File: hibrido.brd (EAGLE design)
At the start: 84 x 62 mm, 14 parts

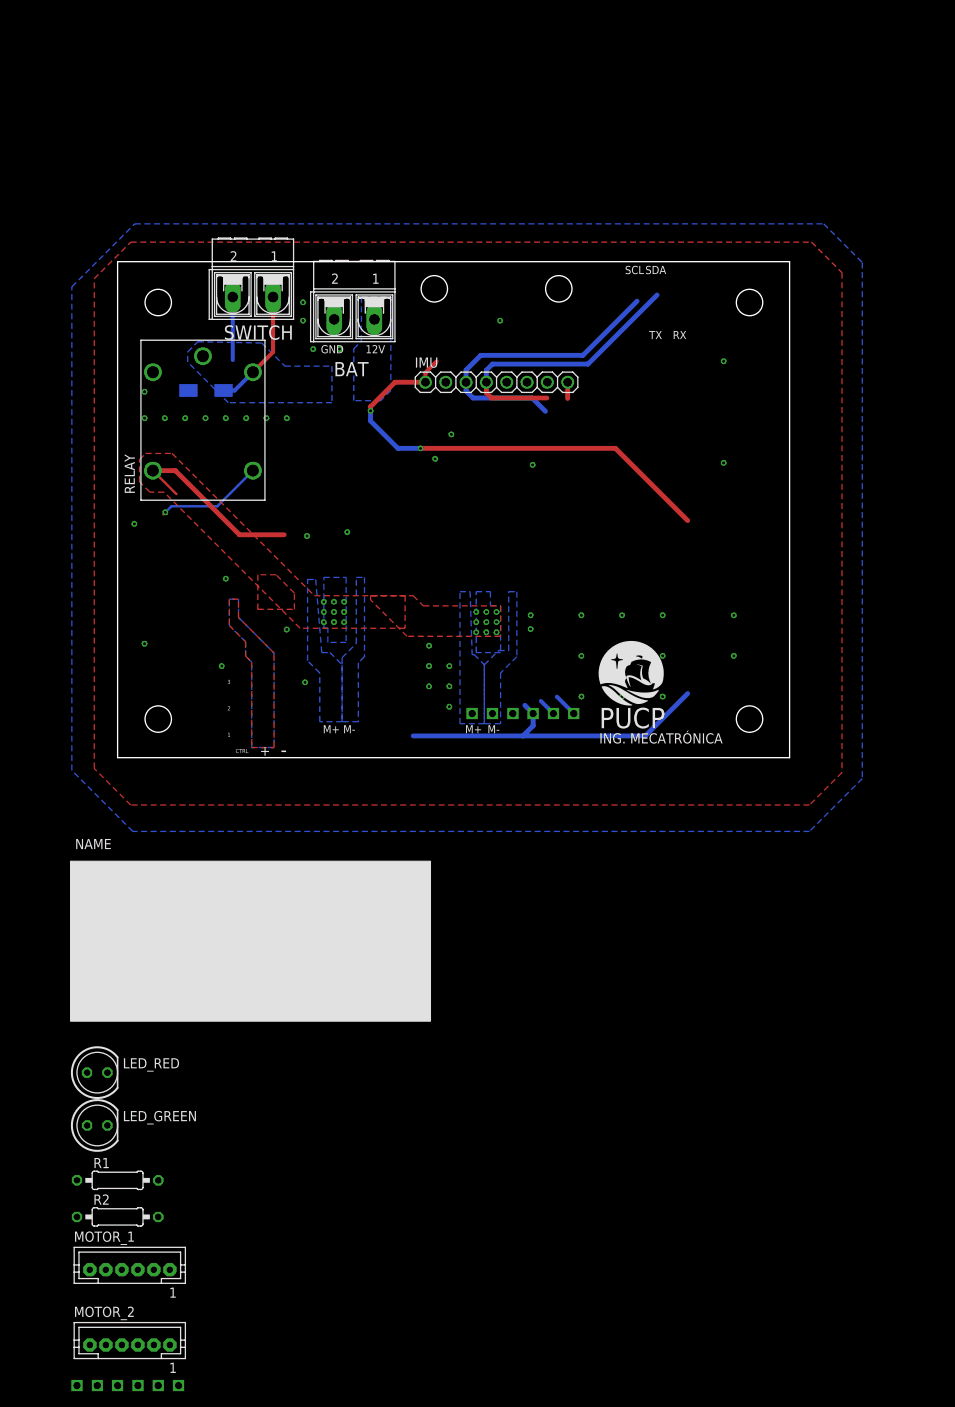
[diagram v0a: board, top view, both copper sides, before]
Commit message: Hibrido casi terminado, sin considerar comunicación entre ESPs
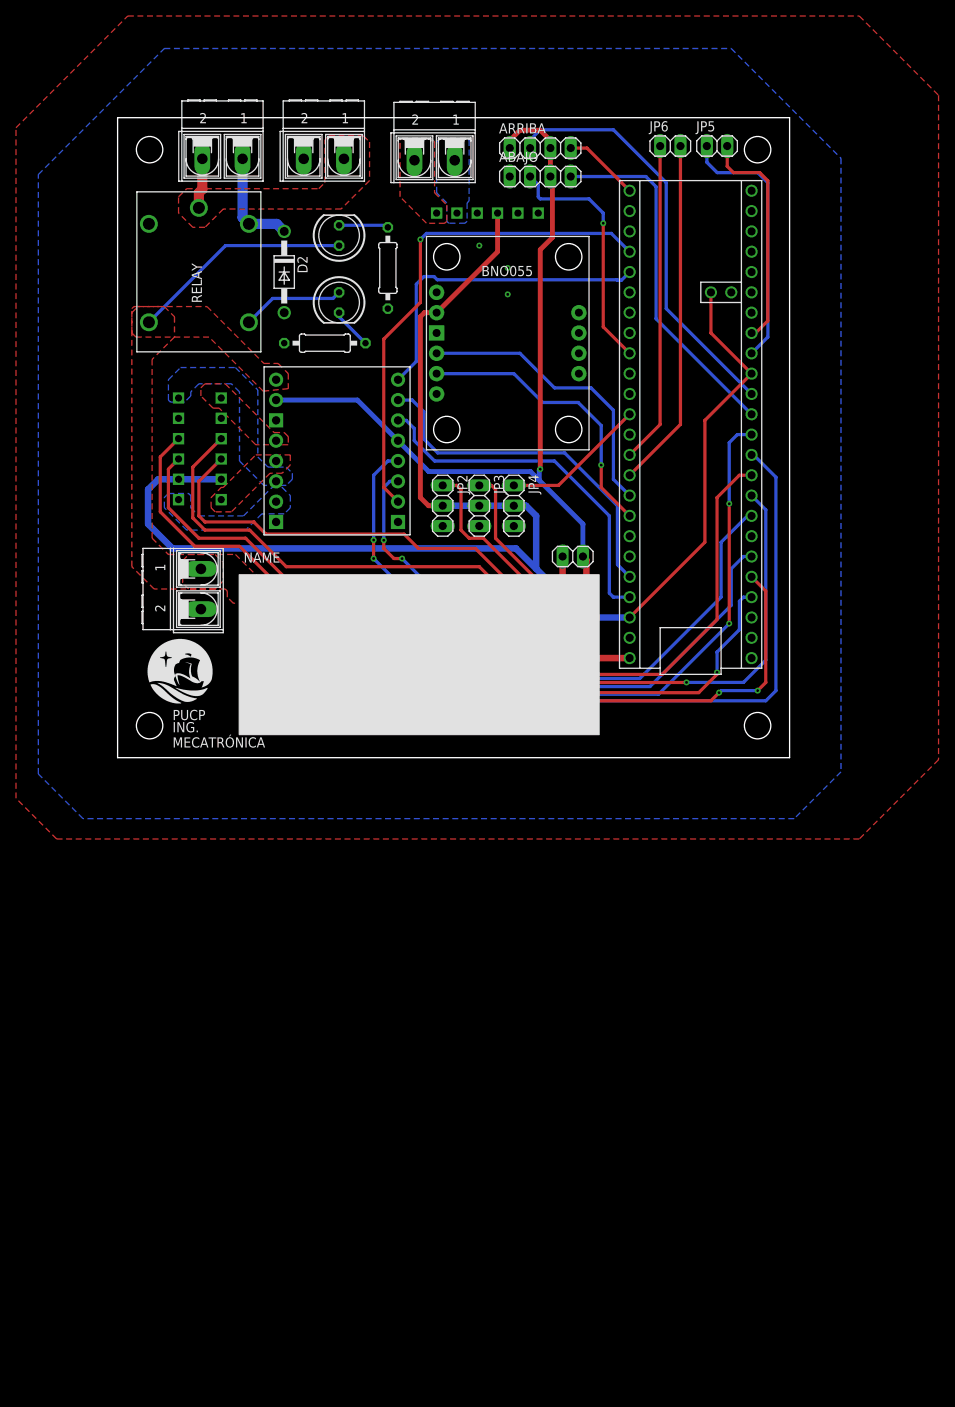
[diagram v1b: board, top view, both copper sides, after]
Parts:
- removed D1: M2, SamacSys_Parts:DIOM5327X250N
- removed IMU: (no value), MPU6050:MPU6050
- removed MOTOR2: MOTOR_JGB370, MOTOR_JGB370:MOTOR_JGB370
- removed MOTOR_1, MOTOR_2: (no value), jst-ph:JST-PH6
- added A1: TEENSY_4.1, TEENSY_4.1:TEENSY_LONG_EXT
- added ABAJO, ARRIBA: (no value), pinhead:1X04
- added ALIMENTACION_DRIVER, DRIVER_HIBRIDACION: (no value), con-ptr500:AK500/2-H
- added BNO055: BNO055, BNO055:BNO055
- added D2: 1N4004, diode:DO41-10
- added JP1, JP5, JP6: (no value), pinhead:1X02
- added JP2, JP3, JP4: (no value), pinhead:1X03
- added MOTOR3, MOTOR5: MOTOR_JGB370, MOTOR_JGB370:MOTOR_JGB370
- added U$3: TB6612FNG, TB6612FNG:TB6612FNG
- moved MOTOR1 152.6 mm to (45.0, 68.1), turned to 180 degrees
- moved R2 123.3 mm to (33.8, 61.2), turned to 90 degrees
- moved LED_GREEN 115.3 mm to (27.7, 65.3), turned to 90 degrees
- moved R1 107.8 mm to (25.9, 51.8)
- moved LED_RED 100.9 mm to (27.7, 56.9), turned to 270 degrees
- moved U$2 41.6 mm to (38.6, 14.2)
- moved BAT 20.4 mm to (25.8, 74.9)
- moved RELAY 18.5 mm to (2.41, 50.7)
- moved SWITCH 17.7 mm to (13.1, 74.9)
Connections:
- net ENAM1 renamed C1_H
- net ENBM1 renamed C2_H
- removed net +3V3: IMU.1, MOTOR1.+5V, MOTOR2.+5V, MOTOR_1.5, MOTOR_2.5
- removed net 16.8V: LED_GREEN.A, RELAY.NO, U$2.IN+
- removed net ENAM2: MOTOR2.ENCB
- removed net ENBM2: MOTOR2.ENCA
- removed net INT_MPU: IMU.8
- removed net MA_1: MOTOR1.MOTOR-
- removed net MA_2: MOTOR2.MOTOR-
- removed net MB_1: MOTOR1.MOTOR+
- removed net MB_2: MOTOR2.MOTOR+
- new net 12V: ALIMENTACION_DRIVER.1, LED_GREEN.A, RELAY.NO, U$2.IN+, U$3.1
- new net 14: A1.D14, JP4.1
- new net 16: A1.D16, JP6.1
- new net 17: A1.D17, JP6.2
- new net 24: A1.D24, JP5.1
- new net 25: A1.D25, JP5.2
- new net 3V3: A1.3V3, A1.3V3@2, A1.3V3@3, BNO055.2, JP2.2, JP3.2, JP4.2, MOTOR1.+5V, MOTOR3.ENCA, MOTOR5.ENCA
- new net 5V: ABAJO.3, ARRIBA.1, ARRIBA.3, JP1.2, U$2.OUT+, U$3.12, U$3.2
- new net 7: A1.D7, JP2.1
- new net 8: A1.D8, JP3.1
- new net AI1: A1.D23, U$3.11
- new net AI2: A1.D22, U$3.10
- new net BI1: A1.D9, U$3.13
- new net BI2: A1.D10, U$3.14
- new net LPWM: A1.D11, ABAJO.4
- new net L_IS: A1.D41, ABAJO.2
- new net N$1: LED_RED.K, R1.2
- new net N$10: A1.D28
- new net N$11: A1.D13
- new net N$19: A1.D5
- new net N$2: A1.D34
- new net N$24: A1.D21
- new net N$25: A1.D20
- new net N$3: A1.D35
- new net N$30: A1.D15
- new net N$33: A1.D40
- new net N$34: A1.D39
- new net N$35: A1.D38
- new net N$38: A1.D26
- new net N$39: A1.D27
- new net N$4: LED_GREEN.K, R2.2
- new net N$6: A1.D32
- new net N$7: A1.D31
- new net N$8: A1.D30
- new net N$9: A1.D29
- new net OUTA: DRIVER_HIBRIDACION.2, MOTOR1.MOTOR+
- new net OUTB: DRIVER_HIBRIDACION.1, MOTOR1.MOTOR-
- new net PWMA: A1.D37, U$3.9
- new net PWMB: A1.D36, U$3.15
- new net RPWM: A1.D33, ARRIBA.4
- new net R_IS: A1.D12, ARRIBA.2
- new net VBAT: A1.VBAT
- new net VIN_TEENSY: A1.VIN, JP1.1
- net A01: now also MOTOR3.MOTOR+, U$3.4; no longer MOTOR_1.1
- net A02: now also MOTOR3.ENCB, U$3.5; no longer MOTOR_1.6
- net B01: now also MOTOR5.ENCB, U$3.7; no longer MOTOR_2.6
- net B02: now also MOTOR5.MOTOR+, U$3.6; no longer MOTOR_2.1
- net C1_L: now also A1.D6, MOTOR5.GND; no longer MOTOR_2.3
- net C1_R: now also A1.D3, MOTOR3.GND; no longer MOTOR_1.3
- net C2_L: now also A1.D4, MOTOR5.+5V; no longer MOTOR_2.4
- net C2_R: now also A1.D2, MOTOR3.+5V; no longer MOTOR_1.4
- net GND: now also A1.AGND/GND, A1.GND, A1.GND@2, ABAJO.1, ALIMENTACION_DRIVER.2, BNO055.3, D2.A, JP2.3, JP3.3, JP4.3, MOTOR3.MOTOR-, MOTOR5.MOTOR-, U$2.OUT-, U$3.16, U$3.3, U$3.8; no longer D1.2, IMU.2, MOTOR2.GND, MOTOR_1.2, MOTOR_2.2
- net SCL: now also A1.D19, BNO055.5; no longer IMU.3
- net SDA: now also A1.D18, BNO055.4; no longer IMU.4
- net VSWITCH: now also D2.C; no longer D1.1
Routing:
- net 3V3: track 0.00 -> 190.6 mm
- net C1_R: track 0.00 -> 115.0 mm, vias 0 -> 2
- net C1_L: track 0.00 -> 105.1 mm, vias 0 -> 1
- net 5V: track 0.00 -> 103.3 mm, vias 0 -> 1
- net BI1: track 0.00 -> 103.3 mm, vias 0 -> 2
- net C2_R: track 0.00 -> 102.5 mm, vias 0 -> 1
- net C2_L: track 0.00 -> 99.2 mm, vias 0 -> 1
- net +3V3: track 99.2 -> 0.00 mm, vias 2 -> 0
- net BI2: track 0.00 -> 89.9 mm, vias 0 -> 4
- net 7: track 0.00 -> 82.0 mm, vias 0 -> 1
- net 8: track 0.00 -> 71.5 mm
- net PWMB: track 0.00 -> 62.8 mm, vias 0 -> 1
- net R_IS: track 0.00 -> 52.1 mm
- net AI1: track 0.00 -> 44.7 mm
- net LPWM: track 0.00 -> 44.6 mm
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- added copper zone on layer 1, net 12V
- added copper zone on layer 1, net A01
- added copper zone on layer 1, net A02
- added copper zone on layer 16, net B01
- added copper zone on layer 16, net B02
- added copper zone on layer 1, net OUTA
- added copper zone on layer 16, net OUTB
- added copper zone on layer 1, net VIN
- removed copper zone on layer 1, net 16.8V
- removed copper zone on layer 16, net 16.8V
- removed copper zone on layer 1, net 6V
- removed copper zone on layer 16, net 6V
- removed copper zone on layer 16, net MA_1
- removed copper zone on layer 16, net MA_2
- removed copper zone on layer 16, net MB_1
- removed copper zone on layer 16, net MB_2
- removed copper zone on layer 16, net VIN
- removed copper zone on layer 16, net V_BAT
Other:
- board size 84 x 62 mm -> 84 x 80 mm
- board text removed: "+"
- board text removed: "-"
- board text removed: "1"
- board text removed: "12V"
- board text removed: "2"
- board text removed: "3"
- board text removed: "CTRL"
- board text removed: "DRIVER"
- board text removed: "GND"
- board text removed: "M+"
- board text removed: "M-"
- board text removed: "RX"
- board text removed: "SCL"
- board text removed: "SDA"
- board text removed: "TX"

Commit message: cambios casi finales
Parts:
- moved ALIMENTACION_DRIVER 0.76 mm to (10.4, 20.3)
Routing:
- net BI2: track 89.9 -> 90.8 mm
- net BI1: track 103.3 -> 104.1 mm
- net C1_L: track 105.1 -> 105.8 mm
- net C2_L: track 99.2 -> 99.8 mm

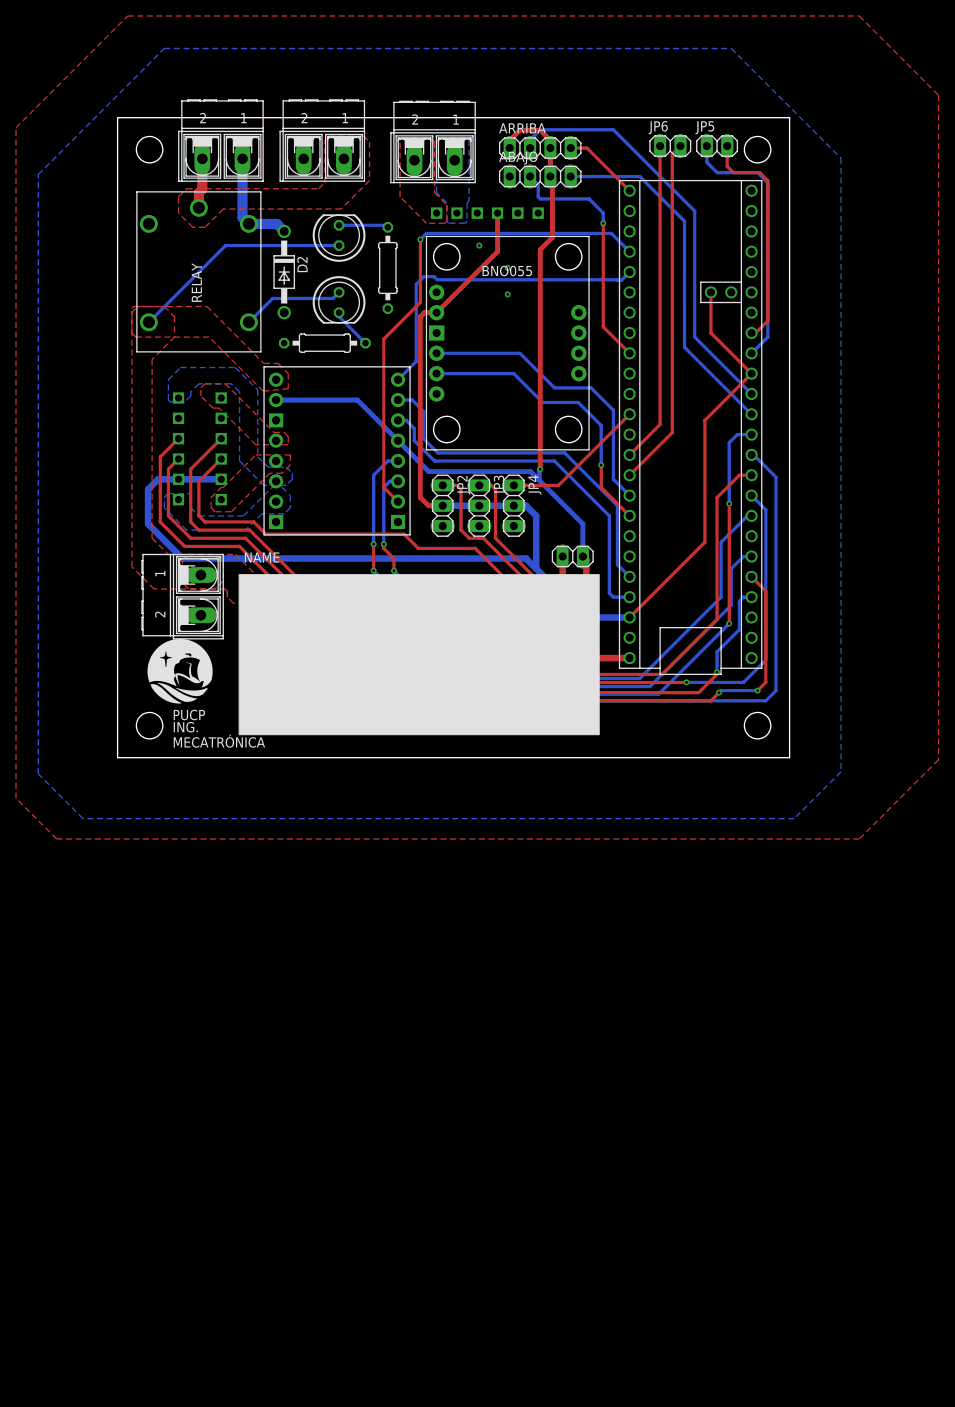
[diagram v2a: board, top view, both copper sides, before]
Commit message: PCB antes del cambio del drill vias
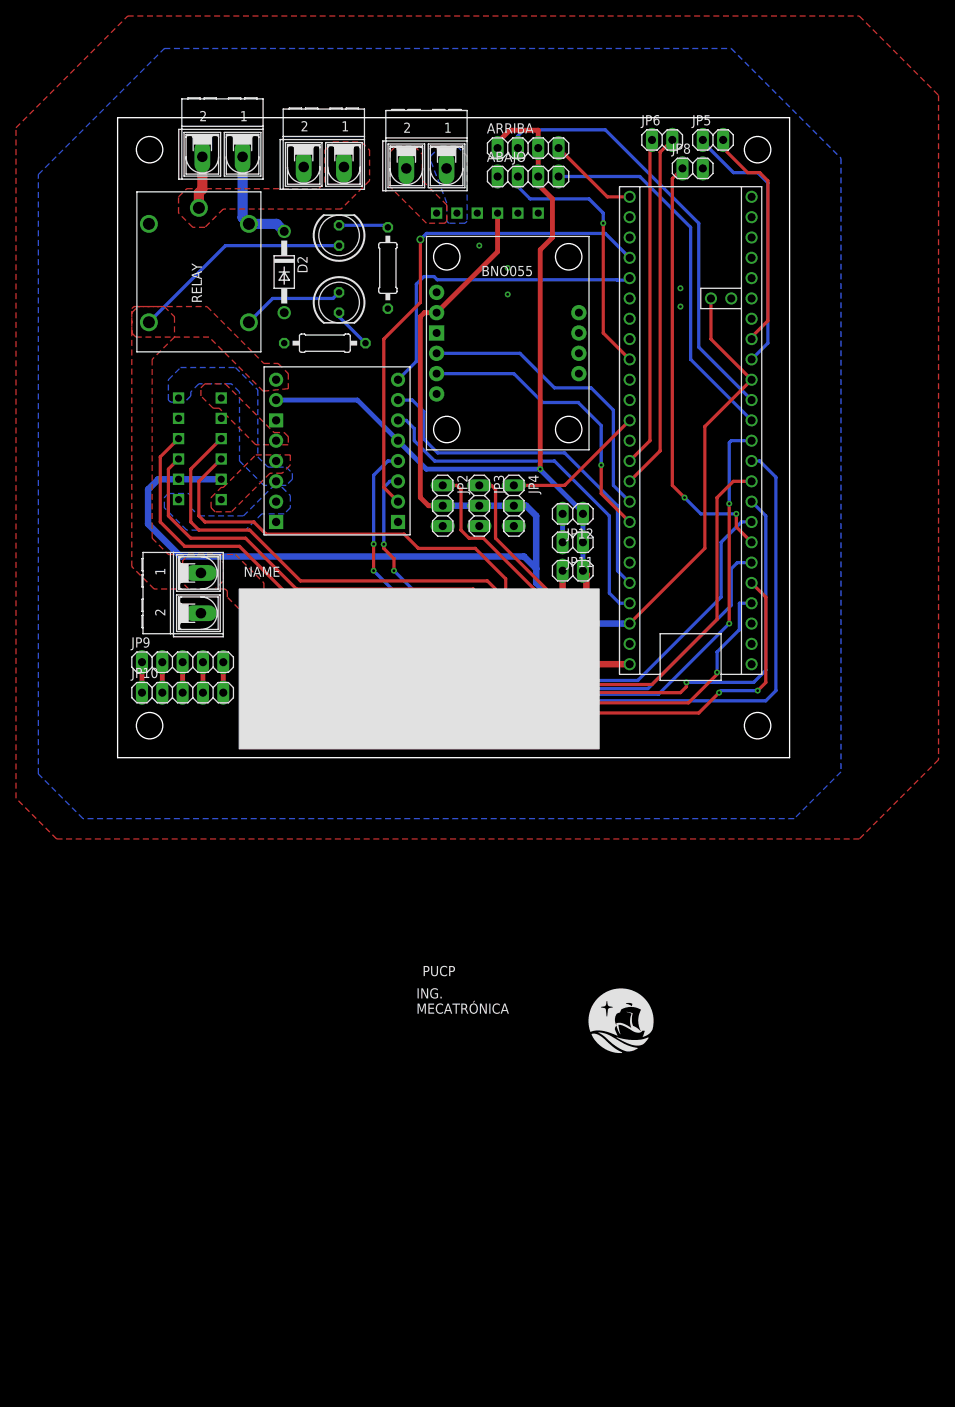
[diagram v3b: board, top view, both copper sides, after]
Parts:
- added JP10, JP9: (no value), pinhead:1X05
- added JP11, JP12, JP8: (no value), pinhead:1X02
- moved JP1 1.78 mm to (56.9, 23.4)
- moved U$2 1.78 mm to (38.6, 12.4)
- moved ABAJO 1.52 mm to (51.3, 72.6)
- moved ARRIBA 1.52 mm to (51.3, 76.2)
- moved DRIVER_HIBRIDACION 1.44 mm to (38.6, 73.7)
- moved JP6 1.27 mm to (68.1, 77.2)
- moved BAT 1.02 mm to (25.8, 73.8)
- moved JP5 0.92 mm to (74.4, 77.2)
- moved A1 0.76 mm to (64.0, 11.7)
- moved SWITCH 0.25 mm to (13.1, 75.1)
- moved ALIMENTACION_DRIVER 0.25 mm to (10.4, 20.6)
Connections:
- removed net N$19: A1.D5
- new net 5: A1.D5, JP8.1
- new net EN_CTRL: JP10.5, JP9.5
- new net MISO: JP10.3, JP9.3
- new net MOSI: JP10.2, JP9.2
- new net SCLK: JP10.1, JP9.1
- new net SS: JP10.4, JP9.4
- net 5V: now also JP11.1, JP12.1
- net GND: now also JP11.2, JP12.2, JP8.2
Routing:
- net 5: track 0.00 -> 54.0 mm, vias 0 -> 2
- net SS: track 0.00 -> 3.81 mm
- net SCLK: track 0.00 -> 3.81 mm
- net MOSI: track 0.00 -> 3.81 mm
- net MISO: track 0.00 -> 3.81 mm
- net EN_CTRL: track 0.00 -> 3.81 mm
- net GND: track 0.00 -> 3.56 mm, vias 3 -> 5
- net 5V: track 103.3 -> 105.7 mm
- net LPWM: track 44.1 -> 46.4 mm
- net L_IS: track 30.8 -> 33.0 mm
- net R_IS: track 52.1 -> 54.1 mm
- net RPWM: track 9.58 -> 11.4 mm
- net VIN_TEENSY: track 19.7 -> 18.3 mm
- net 3V3: track 190.6 -> 191.9 mm
- net 7: track 82.0 -> 83.3 mm
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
